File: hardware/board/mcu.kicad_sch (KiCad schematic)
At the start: 61 parts, among them J301 MidiIn, J302 MidiOut, U301 RP2350_80QFN, U302 THB001P, U303 TLP2310, U304 74AHC1G125DCKR, Y301 ABM8-272-T3

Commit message: fillout LCSC and swap micro usb
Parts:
- D301: LCSC (none) -> C78608
- ENC301, ENC302, ENC303, ENC304, J301, J302: now not fitted
- U301: LCSC (none) -> C39843328
- U302: Availability In Stock -> (none); LCSC (none) -> C2685355; Package None -> (none); Price None -> (none)
- U303: LCSC (none) -> C7473281
- U304: LCSC (none) -> C151890
- Y301: LCSC (none) -> C20625731
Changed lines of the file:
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@@
 			)
 		)
+		(property "LCSC" "C78608"
+			(at 260.35 267.97 90)
+			(hide yes)
+			(show_name no)
+			(do_not_autoplace no)
+			(effects
+				(font
+					(size 1.27 1.27)
+				)
+			)
+		)
 		(pin "2"
 		)
@@
 			)
 		)
+		(property "LCSC" "C7473281"
+			(at 271.78 267.97 0)
+			(hide yes)
+			(show_name no)
+			(do_not_autoplace no)
+			(effects
+				(font
+					(size 1.27 1.27)
+				)
+			)
+		)
 		(pin "1"
 		)
@@
 		(on_board yes)
 		(in_pos_files yes)
-		(dnp no)
+		(dnp yes)
 		(property "Reference" "ENC301"
 			(at 248.666 74.676 90)
@@
 		(on_board yes)
 		(in_pos_files yes)
-		(dnp no)
+		(dnp yes)
 		(fields_autoplaced yes)
 		(property "Reference" "J301"
@@
 			)
 		)
-		(property "Package" "None"
-			(at 350.52 181.61 0)
-			(hide yes)
-			(show_name no)
-			(do_not_autoplace no)
-			(effects
-				(font
-					(size 1.27 1.27)
-				)
-				(justify bottom)
-			)
-		)
-		(property "Price" "None"
-			(at 350.52 181.61 0)
-			(hide yes)
-			(show_name no)
-			(do_not_autoplace no)
-			(effects
-				(font
-					(size 1.27 1.27)
-				)
-				(justify bottom)
-			)
-		)
 		(property "Check_prices" "https://www.snapeda.com/parts/THB001P/C%2526K/view-part/?ref=eda"
 			(at 350.52 181.61 0)
@@
 			)
 		)
-		(property "Availability" "In Stock"
+		(property "MANUFACTURER" "CNK"
 			(at 350.52 181.61 0)
 			(hide yes)
@@
 			)
 		)
-		(property "MANUFACTURER" "CNK"
-			(at 350.52 181.61 0)
+		(property "LCSC" "C2685355"
+			(at 350.52 181.61 90)
 			(hide yes)
 			(show_name no)
@@
 					(size 1.27 1.27)
 				)
-				(justify bottom)
 			)
 		)
@@
 		(on_board yes)
 		(in_pos_files yes)
-		(dnp no)
+		(dnp yes)
 		(property "Reference" "ENC302"
 			(at 296.926 74.676 90)
@@
 			)
 		)
+		(property "LCSC" "C20625731"
+			(at 48.26 197.485 90)
+			(hide yes)
+			(show_name no)
+			(do_not_autoplace no)
+			(effects
+				(font
+					(size 1.27 1.27)
+				)
+			)
+		)
 		(pin "1"
 		)
@@
 			)
 		)
-		(property "Package" "None"
-			(at 379.73 163.83 0)
-			(hide yes)
-			(show_name no)
-			(do_not_autoplace no)
-			(effects
-				(font
-					(size 1.27 1.27)
-				)
-				(justify bottom)
-			)
-		)
-		(property "Price" "None"
-			(at 379.73 163.83 0)
-			(hide yes)
-			(show_name no)
-			(do_not_autoplace no)
-			(effects
-				(font
-					(size 1.27 1.27)
-				)
-				(justify bottom)
-			)
-		)
 		(property "Check_prices" "https://www.snapeda.com/parts/THB001P/C%2526K/view-part/?ref=eda"
 			(at 379.73 163.83 0)
@@
 			)
 		)
-		(property "Availability" "In Stock"
+		(property "MANUFACTURER" "CNK"
 			(at 379.73 163.83 0)
 			(hide yes)
@@
 			)
 		)
-		(property "MANUFACTURER" "CNK"
+		(property "LCSC" "C2685355"
 			(at 379.73 163.83 0)
 			(hide yes)
@@
 					(size 1.27 1.27)
 				)
-				(justify bottom)
 			)
 		)
@@
 			)
 		)
-		(property "Package" "None"
-			(at 350.52 152.4 0)
-			(hide yes)
-			(show_name no)
-			(do_not_autoplace no)
-			(effects
-				(font
-					(size 1.27 1.27)
-				)
-				(justify bottom)
-			)
-		)
-		(property "Price" "None"
-			(at 350.52 152.4 0)
-			(hide yes)
-			(show_name no)
-			(do_not_autoplace no)
-			(effects
-				(font
-					(size 1.27 1.27)
-				)
-				(justify bottom)
-			)
-		)
 		(property "Check_prices" "https://www.snapeda.com/parts/THB001P/C%2526K/view-part/?ref=eda"
 			(at 350.52 152.4 0)
@@
 			)
 		)
-		(property "Availability" "In Stock"
+		(property "MANUFACTURER" "CNK"
 			(at 350.52 152.4 0)
 			(hide yes)
@@
 			)
 		)
-		(property "MANUFACTURER" "CNK"
-			(at 350.52 152.4 0)
+		(property "LCSC" "C2685355"
+			(at 350.52 152.4 90)
 			(hide yes)
 			(show_name no)
@@
 					(size 1.27 1.27)
 				)
-				(justify bottom)
 			)
 		)
@@
 		(on_board yes)
 		(in_pos_files yes)
-		(dnp no)
+		(dnp yes)
 		(property "Reference" "ENC304"
 			(at 393.446 74.676 90)
@@
 		(on_board yes)
 		(in_pos_files yes)
-		(dnp no)
+		(dnp yes)
 		(property "Reference" "J302"
 			(at 294.64 310.5151 0)
@@
 		(on_board yes)
 		(in_pos_files yes)
-		(dnp no)
+		(dnp yes)
 		(property "Reference" "ENC303"
 			(at 345.186 74.676 90)
@@
 			)
 		)
+		(property "LCSC" "C39843328"
+			(at 142.24 111.76 0)
+			(hide yes)
+			(show_name no)
+			(do_not_autoplace no)
+			(effects
+				(font
+					(size 1.27 1.27)
+				)
+			)
+		)
 		(pin "1"
 		)
@@
 			(at 251.46 311.15 0)
 			(hide yes)
+			(show_name no)
+			(do_not_autoplace no)
+			(effects
+				(font
+					(size 1.27 1.27)
+				)
+			)
+		)
+		(property "LCSC" "C151890"
+			(at 251.46 311.15 0)
+			(hide yes)

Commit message: finish LCSC
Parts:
- C301, C303, C304, C305, C306, C307, C308, C309, C310, C311, C312: value 100n -> 100nF; LCSC (none) -> C1525
- C302, C314, C315, C316: value 4.7u -> 4.7uF; LCSC (none) -> C23733
- C313: value 10u -> 10uF; LCSC (none) -> C1713
- C317, C318, C319, C320, C321, C322, C323, C324: LCSC (none) -> C1710
- C325, C326: value 15p -> 15pF; LCSC (none) -> C86285
- C327: LCSC (none) -> C49678
- R301: LCSC (none) -> C25105
- R302, R303, R304, R305, R306, R307, R308, R309, R310, R311, R312, R313, R314, R315, R316, R317: LCSC (none) -> C17414
- R318: LCSC (none) -> C11702
- R319: LCSC (none) -> C17557
- R320: LCSC (none) -> C17634
- R321: LCSC (none) -> C17415

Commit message: inductor lcsc
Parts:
- L301: value 3.3u -> 3.3uF; LCSC (none) -> C42411119
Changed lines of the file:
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@@
 			)
 		)
-		(property "Value" "3.3u"
+		(property "Value" "3.3uF"
 			(at 80.01 76.2 0)
 			(show_name no)
@@
 			(show_name no)
 			(do_not_autoplace no)
+			(effects
+				(font
+					(size 1.27 1.27)
+				)
+			)
+		)
+		(property "LCSC" "C42411119"
+			(at 78.74 74.93 0)
+			(hide yes)
+			(show_name no)
+			(do_not_autoplace no)

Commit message: fix the silkscreens AGAIN!?????????? why are my commits getting overridden
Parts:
- L301: value 3.3uF -> 3.3uH
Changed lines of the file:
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@@
 			)
 		)
-		(property "Value" "3.3uF"
+		(property "Value" "3.3uH"
 			(at 80.01 76.2 0)
 			(show_name no)

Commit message: 3v3out, delete usb, add leds, LDO
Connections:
- net FUSE_ILM: no longer names the net of U301.52 (GPIO41_ADC1)
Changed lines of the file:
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@@
-	(wire
-		(pts
-			(xy 179.07 185.42) (xy 187.96 185.42)
-		)
-		(stroke
-			(width 0)
-			(type default)
-		)
-	)
 	(wire
 		(pts
@@
 		)
 	)
-	(hierarchical_label "FUSE_ILM"
-		(shape input)
-		(at 187.96 185.42 0)
-		(effects
-			(font
-				(size 1.27 1.27)
-			)
-			(justify left)
-		)
-	)

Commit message: some conns
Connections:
- net GND: no longer J301.S
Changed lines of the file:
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@@
-	)
-	(symbol
-		(lib_name "GND_4")
-		(lib_id "power:GND")
-		(at 245.11 274.32 0)
-		(unit 1)
-		(body_style 1)
-		(exclude_from_sim no)
-		(in_bom yes)
-		(on_board yes)
-		(in_pos_files yes)
-		(dnp no)
-		(fields_autoplaced yes)
-		(property "Reference" "#PWR0345"
-			(at 245.11 280.67 0)
-			(hide yes)
-			(show_name no)
-			(do_not_autoplace no)
-			(effects
-				(font
-					(size 1.27 1.27)
-				)
-			)
-		)
-		(property "Value" "GND"
-			(at 245.11 279.4 0)
-			(show_name no)
-			(do_not_autoplace no)
-			(effects
-				(font
-					(size 1.27 1.27)
-				)
-			)
-		)
-		(property "Footprint" ""
-			(at 245.11 274.32 0)
-			(hide yes)
-			(show_name no)
-			(do_not_autoplace no)
-			(effects
-				(font
-					(size 1.27 1.27)
-				)
-			)
-		)
-		(property "Datasheet" ""
-			(at 245.11 274.32 0)
-			(hide yes)
-			(show_name no)
-			(do_not_autoplace no)
-			(effects
-				(font
-					(size 1.27 1.27)
-				)
-			)
-		)
-		(property "Description" "Power symbol creates a global label with name \"GND\" , ground"
-			(at 245.11 274.32 0)
-			(hide yes)
-			(show_name no)
-			(do_not_autoplace no)
-			(effects
-				(font
-					(size 1.27 1.27)
-				)
-			)
-		)
-		(pin "1"
-		)
-		(instances
-			(project "board"
-				(path "/dd13fd41-39ab-4435-9074-5024f1786746/c4d314f2-7502-4a7f-ae5f-cbca93031f6d"
-					(reference "#PWR0345")
-					(unit 1)
-				)
-			)
-		)
 	)
 	(symbol

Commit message: giga test points
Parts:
- added C328: 100nF, Capacitor_SMD:C_0805_2012Metric, symbol Device:C_Small
- added D302: LED Blue, LED_SMD:LED_0603_1608Metric, symbol Device:LED
- added R322: 1k, Resistor_SMD:R_0603_1608Metric_Pad0.98x0.95mm_HandSolder, symbol Device:R
- added TP301: MCU_3V3, symbol Connector:TestPoint
- added TP302: MCU_1V1, symbol Connector:TestPoint
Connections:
- net +1V1: now also TP302.1
- net +3V3: now also C328.1, D302.2 (A), TP301.1
- net GND: now also C328.2
- net HEARTBEAT: now reaches U301.48 (GPIO39)
- net HEARTBEAT: now also R322.2
- new net: D302.1 (K), R322.1
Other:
- note added: "Activity LED"

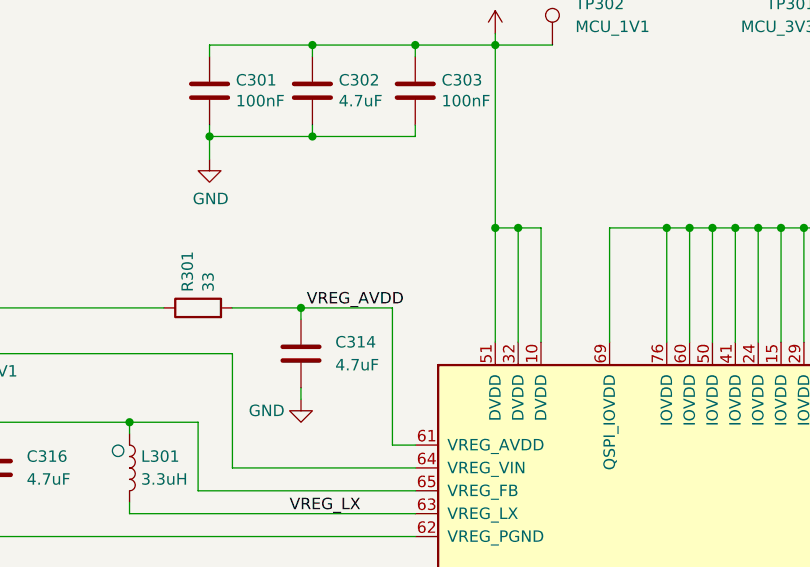
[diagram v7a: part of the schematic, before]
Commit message: barrel jack and power conns
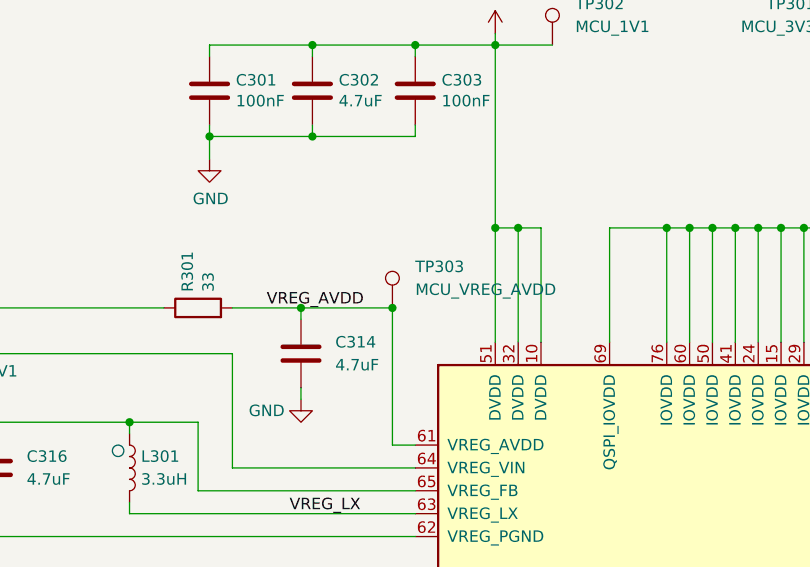
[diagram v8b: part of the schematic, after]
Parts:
- added TP303: MCU_VREG_AVDD, symbol Connector:TestPoint
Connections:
- net VREG_AVDD: now also TP303.1
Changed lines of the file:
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@@
 	)
 	(junction
+		(at 107.95 57.15)
+		(diameter 0)
+		(color 0 0 0 0)
+	)
+	(junction
 		(at 246.38 107.95)
 		(diameter 0)
@@
 	(wire
 		(pts
-			(xy 90.17 57.15) (xy 97.79 57.15)
+			(xy 90.17 57.15) (xy 107.95 57.15)
 		)
 		(stroke
@@
 	(wire
 		(pts
-			(xy 97.79 57.15) (xy 107.95 57.15)
-		)
-		(stroke
-			(width 0)
-			(type default)
-		)
-	)
-	(wire
-		(pts
 			(xy 320.04 99.06) (xy 309.88 99.06)
 		)
@@
 	)
 	(label "VREG_AVDD"
-		(at 98.425 57.15 0)
+		(at 93.98 57.15 0)
 		(effects
 			(font
@@
 					(unit 1)
 				)
+			)
+		)
+	)
+	(symbol
+		(lib_id "Connector:TestPoint")
+		(at 107.95 57.15 0)
+		(unit 1)
+		(body_style 1)
+		(exclude_from_sim no)
+		(in_bom yes)
+		(on_board yes)
+		(in_pos_files yes)
+		(dnp no)
+		(property "Reference" "TP303"
+			(at 110.49 52.5779 0)
+			(show_name no)
+			(do_not_autoplace no)
+			(effects
+				(font
+					(size 1.27 1.27)
+				)
+				(justify left)
+			)
+		)
+		(property "Value" "MCU_VREG_AVDD"
+			(at 110.49 55.1179 0)
+			(show_name no)
+			(do_not_autoplace no)
+			(effects
+				(font
+					(size 1.27 1.27)
+				)
+				(justify left)
+			)
+		)
+		(property "Footprint" ""
+			(at 113.03 57.15 0)
+			(hide yes)
+			(show_name no)
+			(do_not_autoplace no)
+			(effects
+				(font
+					(size 1.27 1.27)
+				)
+			)
+		)
+		(property "Datasheet" ""
+			(at 113.03 57.15 0)
+			(hide yes)
+			(show_name no)
+			(do_not_autoplace no)
+			(effects
+				(font
+					(size 1.27 1.27)
+				)
+			)
+		)
+		(property "Description" "test point"
+			(at 107.95 57.15 0)
+			(hide yes)
+			(show_name no)
+			(do_not_autoplace no)
+			(effects
+				(font
+					(size 1.27 1.27)
+				)
+			)
+		)
+		(pin "1"
+		)
+		(instances
+			(project "board"
+				(path "/dd13fd41-39ab-4435-9074-5024f1786746/c4d314f2-7502-4a7f-ae5f-cbca93031f6d"
+					(reference "TP303")
+					(unit 1)
+				)
